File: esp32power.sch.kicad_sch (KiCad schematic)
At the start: 39 parts, among them J1 6120XX21621_61201021621, Q1 MMBT3904, Q2 MMBT3904, U10 TL072, U11 TL072, U2 TPS72301DDC, U3 R-78E3.3-1.0, U5 NAU88C22YG, U6 TPS72301DDC, U7 TL072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

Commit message: updatedlibrary location
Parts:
- removed unit 1 of U10
- added FL2: BLM21PG221SN1D, customfootprints:bead, symbol esp32lib:bead
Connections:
- net +12V: now also FL2.1, FL2.2
- net -3V3: now reaches C13.2, R10.2, U10.7

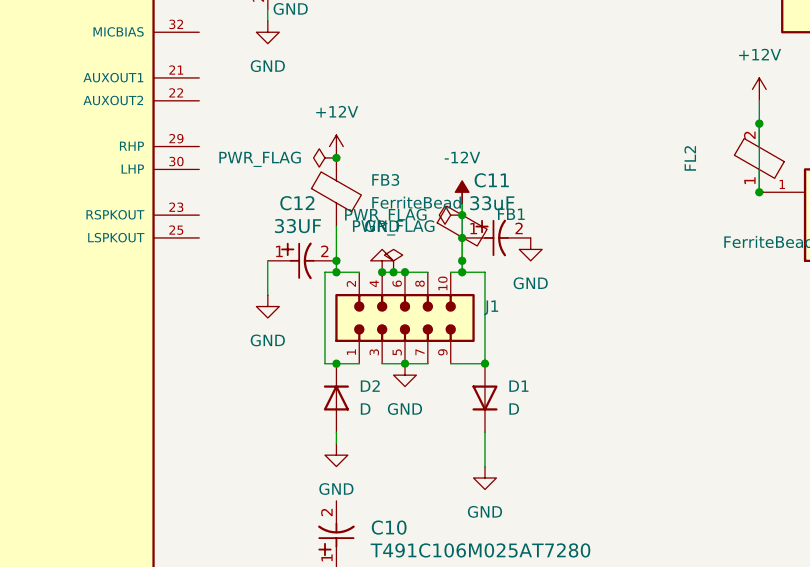
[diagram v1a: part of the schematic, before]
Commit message: added some power flags and cleaned up power stuff
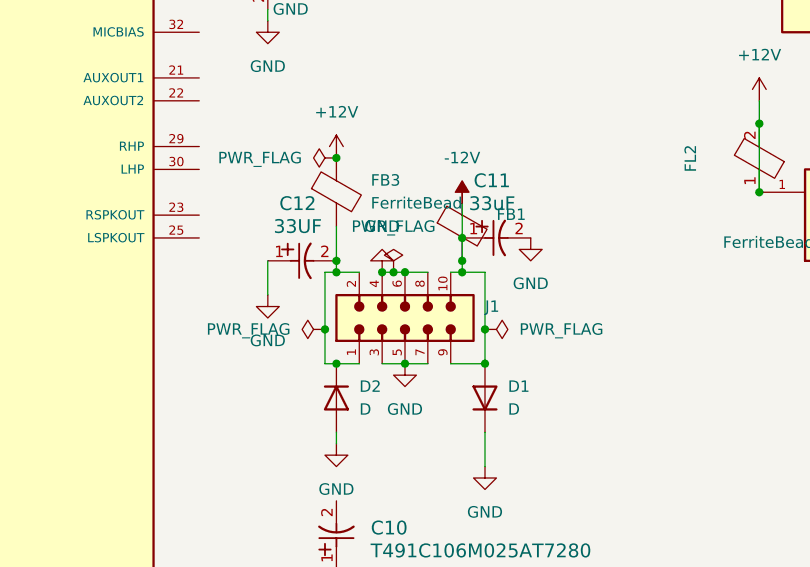
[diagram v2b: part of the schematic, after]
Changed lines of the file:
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@@
 	)
 	(junction
+		(at 153.67 107.95)
+		(diameter 0)
+		(color 0 0 0 0)
+	)
+	(junction
 		(at 151.13 97.79)
 		(diameter 0)
@@
 	)
 	(junction
-		(at 151.13 95.25)
-		(diameter 0)
-		(color 0 0 0 0)
-	)
-	(junction
 		(at 210.82 146.05)
 		(diameter 0)
@@
 	)
 	(junction
+		(at 135.89 107.95)
+		(diameter 0)
+		(color 0 0 0 0)
+	)
+	(junction
 		(at 137.16 101.6)
 		(diameter 0)
@@
 	(wire
 		(pts
-			(xy 135.89 111.76) (xy 135.89 101.6)
+			(xy 135.89 111.76) (xy 135.89 107.95)
 		)
 		(stroke
@@
 	(wire
 		(pts
-			(xy 151.13 95.25) (xy 151.13 97.79)
+			(xy 151.13 93.98) (xy 151.13 97.79)
 		)
 		(stroke
@@
 	(wire
 		(pts
+			(xy 153.67 107.95) (xy 153.67 111.76)
+		)
+		(stroke
+			(width 0)
+			(type default)
+		)
+	)
+	(wire
+		(pts
 			(xy 139.7 111.76) (xy 137.16 111.76)
 		)
@@
 	(wire
 		(pts
-			(xy 151.13 93.98) (xy 151.13 95.25)
-		)
-		(stroke
-			(width 0)
-			(type default)
-		)
-	)
-	(wire
-		(pts
 			(xy 231.14 57.15) (xy 231.14 62.23)
 		)
@@
 	(wire
 		(pts
+			(xy 135.89 107.95) (xy 135.89 101.6)
+		)
+		(stroke
+			(width 0)
+			(type default)
+		)
+	)
+	(wire
+		(pts
 			(xy 233.68 80.01) (xy 215.9 80.01)
 		)
@@
 	(wire
 		(pts
-			(xy 153.67 101.6) (xy 153.67 111.76)
+			(xy 153.67 101.6) (xy 153.67 107.95)
 		)
 		(stroke
@@
 	)
 	(symbol
+		(lib_id "power:PWR_FLAG")
+		(at 153.67 107.95 270)
+		(unit 1)
+		(exclude_from_sim no)
+		(in_bom yes)
+		(on_board yes)
+		(dnp no)
+		(fields_autoplaced yes)
+		(property "Reference" "#FLG4"
+			(at 155.575 107.95 0)
+			(effects
+				(font
+					(size 1.27 1.27)
+				)
+				(hide yes)
+			)
+		)
+		(property "Value" "PWR_FLAG"
+			(at 157.48 107.9499 90)
+			(effects
+				(font
+					(size 1.27 1.27)
+				)
+				(justify left)
+			)
+		)
+		(property "Footprint" ""
+			(at 153.67 107.95 0)
+			(effects
+				(font
+					(size 1.27 1.27)
+				)
+				(hide yes)
+			)
+		)
+		(property "Datasheet" "~"
+			(at 153.67 107.95 0)
+			(effects
+				(font
+					(size 1.27 1.27)
+				)
+				(hide yes)
+			)
+		)
+		(property "Description" "Special symbol for telling ERC where power comes from"
+			(at 153.67 107.95 0)
+			(effects
+				(font
+					(size 1.27 1.27)
+				)
+				(hide yes)
+			)
+		)
+		(pin "1"
+		)
+		(instances
+			(project "esp32"
+				(path "/c4754426-a41b-4341-9d09-2e389619f3d6/4920d9cc-53c2-4c88-995f-b1115cf9bcec"
+					(reference "#FLG4")
+					(unit 1)
+				)
+			)
+		)
+	)
+	(symbol
 		(lib_id "Device:D")
 		(at 153.67 115.57 90)
@@
 	)
 	(symbol
-		(lib_id "power:PWR_FLAG")
-		(at 151.13 95.25 90)
-		(unit 1)
-		(exclude_from_sim no)
-		(in_bom yes)
-		(on_board yes)
-		(dnp no)
-		(fields_autoplaced yes)
-		(property "Reference" "#FLG4"
-			(at 149.225 95.25 0)
-			(effects
-				(font
-					(size 1.27 1.27)
-				)
-				(hide yes)
-			)
-		)
-		(property "Value" "PWR_FLAG"
-			(at 147.32 95.2499 90)
-			(effects
-				(font
-					(size 1.27 1.27)
-				)
-				(justify left)
-			)
-		)
-		(property "Footprint" ""
-			(at 151.13 95.25 0)
-			(effects
-				(font
-					(size 1.27 1.27)
-				)
-				(hide yes)
-			)
-		)
-		(property "Datasheet" "~"
-			(at 151.13 95.25 0)
-			(effects
-				(font
-					(size 1.27 1.27)
-				)
-				(hide yes)
-			)
-		)
-		(property "Description" "Special symbol for telling ERC where power comes from"
-			(at 151.13 95.25 0)
-			(effects
-				(font
-					(size 1.27 1.27)
-				)
-				(hide yes)
-			)
-		)
-		(pin "1"
-		)
-		(instances
-			(project ""
-				(path "/c4754426-a41b-4341-9d09-2e389619f3d6/4920d9cc-53c2-4c88-995f-b1115cf9bcec"
-					(reference "#FLG4")
-					(unit 1)
-				)
-			)
-		)
-	)
-	(symbol
 		(lib_id "power:GND")
 		(at 132.08 67.31 0)
@@
 					(unit 1)
 				)
+			)
+		)
+	)
+	(symbol
+		(lib_id "power:PWR_FLAG")
+		(at 135.89 107.95 90)
+		(unit 1)
+		(exclude_from_sim no)
+		(in_bom yes)
+		(on_board yes)
+		(dnp no)
+		(fields_autoplaced yes)
+		(property "Reference" "#FLG6"
+			(at 133.985 107.95 0)
+			(effects
+				(font
+					(size 1.27 1.27)
+				)
+				(hide yes)
+			)
+		)
+		(property "Value" "PWR_FLAG"
+			(at 132.08 107.9499 90)
+			(effects
+				(font
+					(size 1.27 1.27)
+				)
+				(justify left)
+			)
+		)
+		(property "Footprint" ""
+			(at 135.89 107.95 0)
+			(effects
+				(font
+					(size 1.27 1.27)
+				)
+				(hide yes)
+			)
+		)
+		(property "Datasheet" "~"
+			(at 135.89 107.95 0)
+			(effects
+				(font
+					(size 1.27 1.27)
+				)
+				(hide yes)
+			)
+		)
+		(property "Description" "Special symbol for telling ERC where power comes from"
+			(at 135.89 107.95 0)
+			(effects
+				(font
+					(size 1.27 1.27)
+				)
+				(hide yes)
+			)
+		)
+		(pin "1"
+		)
+		(instances
+			(project "esp32"
+				(path "/c4754426-a41b-4341-9d09-2e389619f3d6/4920d9cc-53c2-4c88-995f-b1115cf9bcec"
+					(reference "#FLG6")
+					(unit 1)
+				)

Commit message: powersupply added
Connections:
- net VDD: now also C1.1, C7.1, R9.1, U3.3 (OUT)
- net VDDA: no longer C1.1, C7.1, R9.1, U3.3 (OUT)

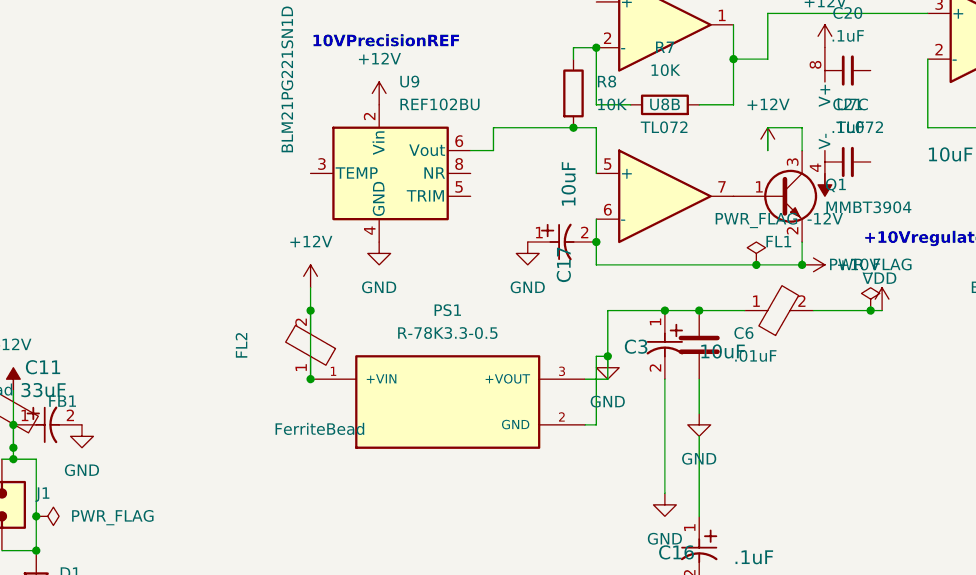
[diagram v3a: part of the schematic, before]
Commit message: UPDATED AU88 CODEC PINS
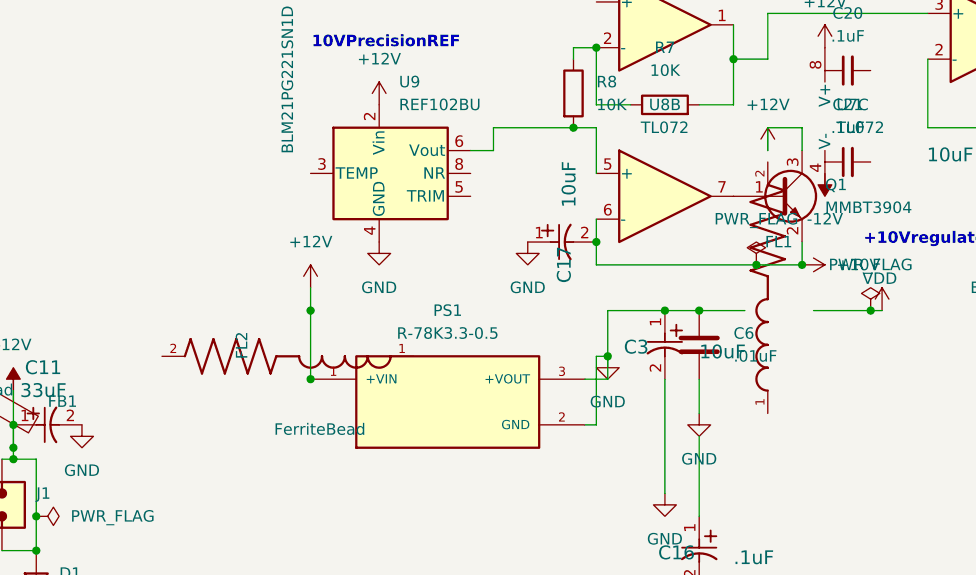
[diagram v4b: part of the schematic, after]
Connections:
- net +12V: no longer FL2.1, FL2.2
- net GND: no longer FL1.1
- net VDD: no longer FL1.2

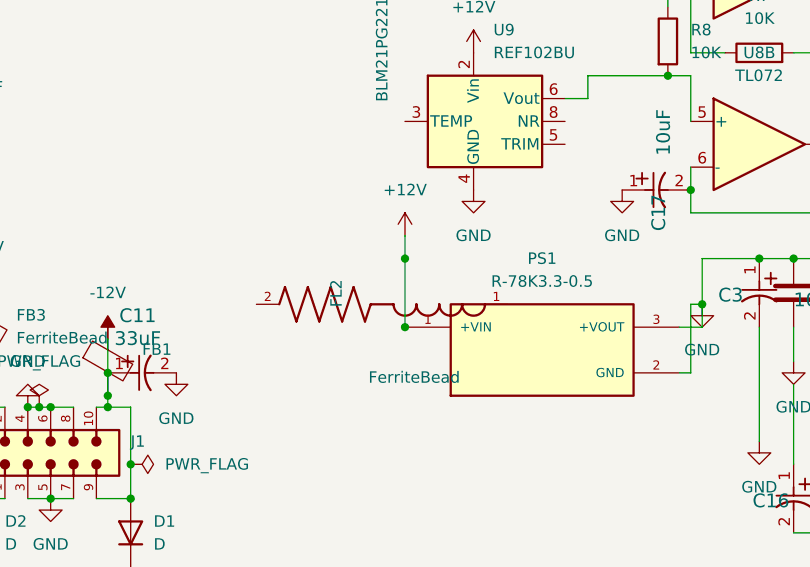
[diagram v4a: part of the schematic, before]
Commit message: added codec buffers
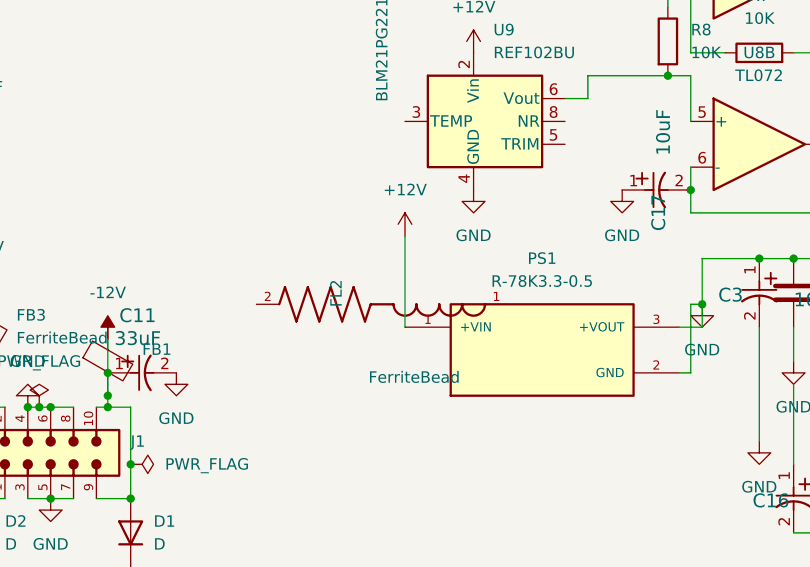
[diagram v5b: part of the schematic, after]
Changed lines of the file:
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@@
-	)
-	(junction
-		(at 184.15 85.09)
-		(diameter 0)
-		(color 0 0 0 0)
 	)
 	(junction
@@
 	)
 	(junction
-		(at 184.15 92.71)
-		(diameter 0)
-		(color 0 0 0 0)
-	)
-	(junction
 		(at 135.89 107.95)
 		(diameter 0)
@@
 	(wire
 		(pts
-			(xy 184.15 92.71) (xy 184.15 85.09)
+			(xy 184.15 82.55) (xy 184.15 92.71)
 		)
 		(stroke
@@
 		)
 		(stroke
-			(width 0)
-			(type default)
-		)
-	)
-	(wire
-		(pts
-			(xy 184.15 82.55) (xy 184.15 85.09)
-		)
-		(stroke

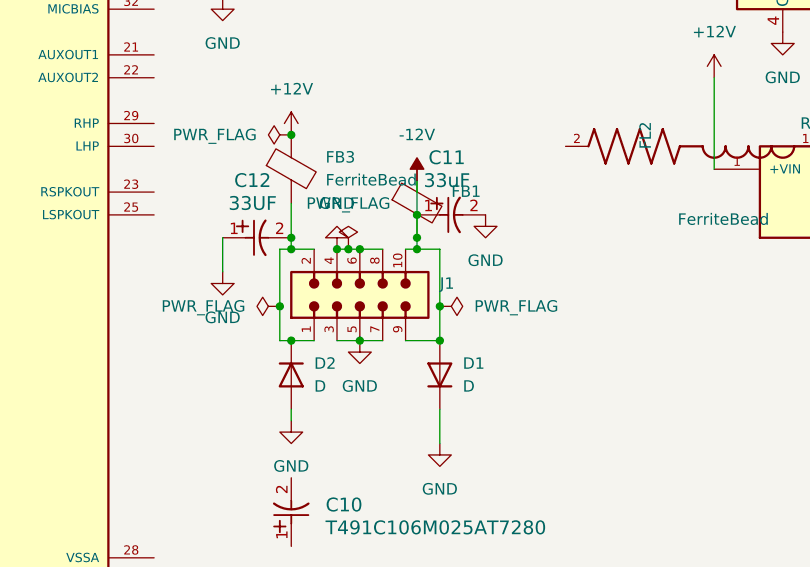
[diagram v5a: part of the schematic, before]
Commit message: added global library
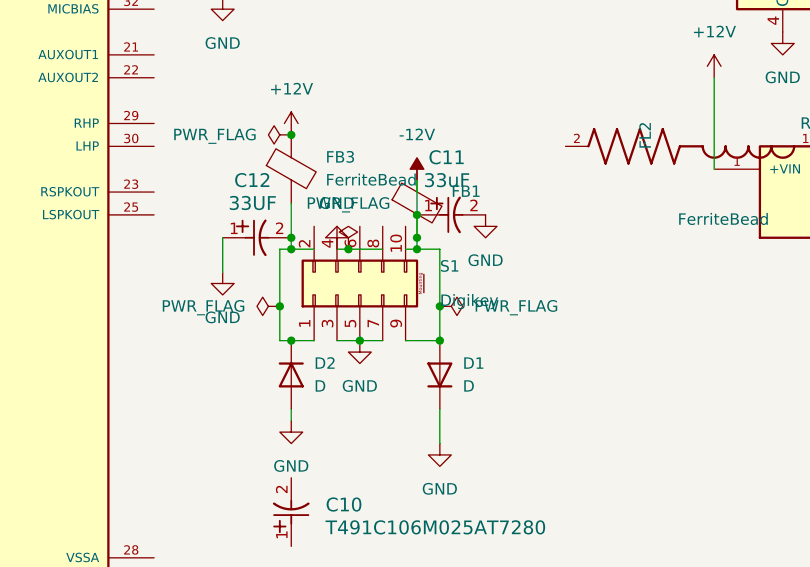
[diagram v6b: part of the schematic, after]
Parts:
- removed J1: 6120XX21621_61201021621, customfootprints:2x5header, symbol esp32lib:header2x5
- added S1: ~, customfootprints:2x5header, symbol common:euroHeader
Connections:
- net -12V: now also S1.9
- net GND: now also S1.3, S1.5, S1.7
- net at C12.2, D2.1 (K), FB3.2: now also S1.1
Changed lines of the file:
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@@
 	)
 	(junction
-		(at 144.78 101.6)
-		(diameter 0)
-		(color 0 0 0 0)
-	)
-	(junction
 		(at 223.52 85.09)
 		(diameter 0)
@@
 	)
 	(junction
-		(at 142.24 101.6)
-		(diameter 0)
-		(color 0 0 0 0)
-	)
-	(junction
 		(at 275.59 63.5)
 		(diameter 0)
@@
 	(wire
 		(pts
-			(xy 143.51 101.6) (xy 144.78 101.6)
+			(xy 143.51 101.6) (xy 147.32 101.6)
 		)
 		(stroke
@@
 	(wire
 		(pts
-			(xy 144.78 101.6) (xy 147.32 101.6)
-		)
-		(stroke
-			(width 0)
-			(type default)
-		)
-	)
-	(wire
-		(pts
 			(xy 240.03 85.09) (xy 246.38 85.09)
 		)
@@
 	)
 	(symbol
-		(lib_id "esp32lib:header2x5")
-		(at 144.78 106.68 0)
-		(unit 1)
-		(exclude_from_sim no)
-		(in_bom yes)
-		(on_board yes)
-		(dnp no)
-		(fields_autoplaced yes)
-		(property "Reference" "J1"
-			(at 153.67 105.4099 0)
-			(effects
-				(font
-					(size 1.27 1.27)
-				)
-				(justify left)
-			)
-		)
-		(property "Value" "6120XX21621_61201021621"
-			(at 153.67 107.9499 0)
-			(effects
-				(font
-					(size 1.27 1.27)
-				)
-				(justify left)
-				(hide yes)
-			)
-		)
-		(property "Footprint" "customfootprints:2x5header"
-			(at 144.78 106.68 0)
-			(effects
-				(font
-					(size 1.27 1.27)
-				)
-				(justify bottom)
-				(hide yes)
-			)
-		)
-		(property "Datasheet" ""
-			(at 144.78 106.68 0)
-			(effects
-				(font
-					(size 1.27 1.27)
-				)
-				(hide yes)
-			)
-		)
-		(property "Description" ""
-			(at 144.78 106.68 0)
-			(effects
-				(font
-					(size 1.27 1.27)
-				)
-				(hide yes)
-			)
-		)
-		(pin "3"
-		)
-		(pin "10"
-		)
-		(pin "7"
-		)
-		(pin "9"
-		)
-		(pin "2"
-		)
-		(pin "6"
-		)
-		(pin "1"
-		)
-		(pin "5"
-		)
-		(pin "4"
-		)
-		(pin "8"
-		)
-		(instances
-			(project ""
-				(path "/c4754426-a41b-4341-9d09-2e389619f3d6/4920d9cc-53c2-4c88-995f-b1115cf9bcec"
-					(reference "J1")
-					(unit 1)
-				)
-				(path "/c4754426-a41b-4341-9d09-2e389619f3d6/32d637b3-b81c-4082-b7fa-739e0cc157fd/f9988e3c-4c3b-480a-910f-ba6be8b52116"
-					(reference "J1")
-					(unit 1)
-				)
-			)
-		)
-	)
-	(symbol
 		(lib_id "Amplifier_Operational:TL072")
 		(at 250.19 144.78 0)
@@
 					(unit 1)
 				)
+			)
+		)
+	)
+	(symbol
+		(lib_id "common:euroHeader")
+		(at 139.7 118.11 90)
+		(unit 1)
+		(exclude_from_sim no)
+		(in_bom yes)
+		(on_board yes)
+		(dnp no)
+		(fields_autoplaced yes)
+		(property "Reference" "S1"
+			(at 153.67 103.5049 90)
+			(effects
+				(font
+					(size 1.27 1.27)
+				)
+				(justify right)
+			)
+		)
+		(property "Value" "~"
+			(at 153.67 105.41 90)
+			(effects
+				(font
+					(size 1.27 1.27)
+				)
+				(justify right)
+			)
+		)
+		(property "Footprint" "customfootprints:2x5header"
+			(at 133.604 117.094 0)
+			(effects
+				(font
+					(size 1.27 1.27)
+				)
+				(hide yes)
+			)
+		)
+		(property "Datasheet" ""
+			(at 139.7 118.11 0)
+			(effects
+				(font
+					(size 1.27 1.27)
+				)
+				(hide yes)
+			)
+		)
+		(property "Description" ""
+			(at 139.7 118.11 0)
+			(effects
+				(font
+					(size 1.27 1.27)
+				)
+				(hide yes)
+			)
+		)
+		(property "MFP#" "CONN HEADER VERT 12POS 2.54MM"
+			(at 136.144 119.634 0)
+			(do_not_autoplace yes)
+			(effects
+				(font
+					(size 1.27 1.27)
+				)
+				(hide yes)
+			)
+		)
+		(property "supplier" "Digikey"
+			(at 153.67 107.3149 90)
+			(effects
+				(font
+					(size 1.27 1.27)
+				)
+				(justify right)
+			)
+		)
+		(property "sup#" "23-0702461201-ND"
+			(at 139.7 118.11 0)
+			(effects
+				(font
+					(size 1.27 1.27)
+				)
+				(hide yes)
+			)
+		)
+		(pin "8"
+		)
+		(pin "10"
+		)
+		(pin "3"
+		)
+		(pin "2"
+		)
+		(pin "6"
+		)
+		(pin "1"
+		)
+		(pin "4"
+		)
+		(pin "5"
+		)
+		(pin "9"
+		)
+		(pin "7"
+		)
+		(instances
+			(project ""
+				(path "/c4754426-a41b-4341-9d09-2e389619f3d6/4920d9cc-53c2-4c88-995f-b1115cf9bcec"
+					(reference "S1")
+					(unit 1)
+				)
+				(path "/c4754426-a41b-4341-9d09-2e389619f3d6/32d637b3-b81c-4082-b7fa-739e0cc157fd/f9988e3c-4c3b-480a-910f-ba6be8b52116"
+					(reference "S2")
+					(unit 1)
+				)
